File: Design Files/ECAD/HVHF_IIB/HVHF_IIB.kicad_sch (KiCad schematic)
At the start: 53 parts, among them J1 1984963, J2 1984963, J3 731375003, J4 CONSMA002-L, Q1 PNP, Q2 BFP196E6327HTSA1, T1 BFU590G, T10 BFQ252, T11 BFQ252, T12 BFQ252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

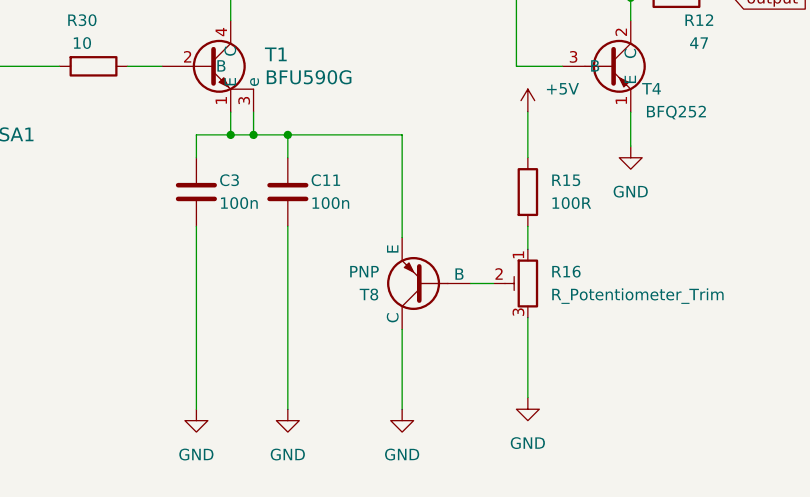
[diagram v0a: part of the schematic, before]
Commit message: adds footprints
3d models
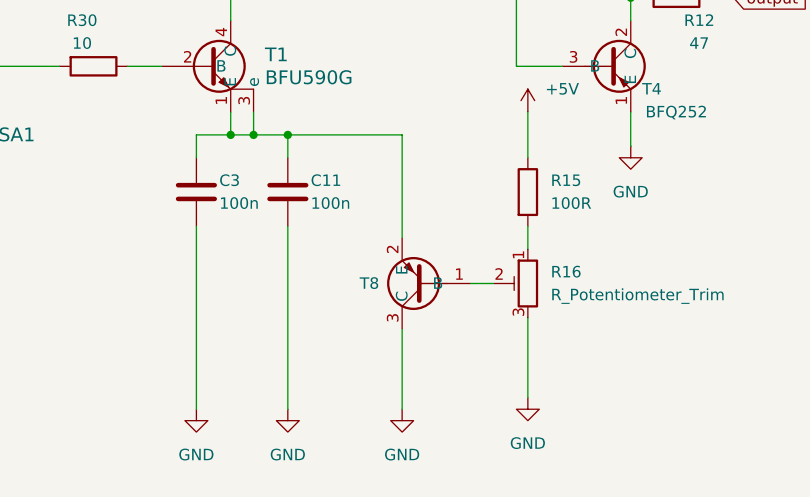
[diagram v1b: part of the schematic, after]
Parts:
- removed T8: PNP, symbol Simulation_SPICE:PNP
- added T8: ~, Package_TO_SOT_SMD:SOT-23, symbol New_Library:PMBT2907A
- R11: footprint Library:PWR163 DPAK -> Library:PWWR0016
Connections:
- net GND: now also T8.3 (C)
- net at R16.2: now also T8.1 (B)
- net at C11.1, C3.1, T1.1 (E)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: now also T8.2 (E)
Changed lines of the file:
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@@
       (effects (font (size 1.27 1.27)) (justify left))
     )
-    (property "Footprint" "Library:PWR163 DPAK" (at 104.902 91.44 90)
+    (property "Footprint" "Library:PWWR0016" (at 104.902 91.44 90)
       (effects (font (size 1.27 1.27)) hide)
     )
@@
     )
   )
+  (symbol (lib_id "New_Library:PMBT2907A") (at 139.7 172.72 180) (unit 1)
+    (in_bom yes) (on_board yes) (dnp no) (fields_autoplaced)
+    (property "Reference" "T8" (at 135.89 172.72 0)
+      (effects (font (size 1.27 1.27)) (justify left))
+    )
+    (property "Value" "~" (at 139.7 172.72 0)
+      (effects (font (size 1.27 1.27)))
+    )
+    (property "Footprint" "Package_TO_SOT_SMD:SOT-23" (at 139.7 172.72 0)
+      (effects (font (size 1.27 1.27)) hide)
+    )
+    (property "Datasheet" "" (at 139.7 172.72 0)
+      (effects (font (size 1.27 1.27)) hide)
+    )
+    (pin "1")
+    (pin "2")
+    (pin "3")
+    (instances
+      (project "HVHF_IIB"
+        (path "/a4785c7b-64d4-4462-915b-801e602c6997"
+          (reference "T8") (unit 1)
+        )
+      )
+    )
+  )
   (symbol (lib_id "Device:R") (at 142.24 114.3 270) (unit 1)
     (in_bom yes) (on_board yes) (dnp no) (fields_autoplaced)
@@
         )
       )
-    )
-  )
-  (symbol (lib_id "Simulation_SPICE:PNP") (at 140.97 172.72 180) (unit 1)
-    (in_bom yes) (on_board yes) (dnp no)
-    (property "Reference" "T8" (at 135.89 173.99 0)
-      (effects (font (size 1.27 1.27)) (justify left))
-    )
-    (property "Value" "PNP" (at 135.89 171.45 0)
-      (effects (font (size 1.27 1.27)) (justify left))
-    )
-    (property "Footprint" "" (at 105.41 172.72 0)
-      (effects (font (size 1.27 1.27)) hide)
-    )
-    (property "Datasheet" "~" (at 105.41 172.72 0)
-      (effects (font (size 1.27 1.27)) hide)
-    )
-    (property "Sim.Device" "PNP" (at 140.97 172.72 0)
-      (effects (font (size 1.27 1.27)) hide)
-    )
-    (property "Sim.Type" "GUMMELPOON" (at 140.97 172.72 0)
-      (effects (font (size 1.27 1.27)) hide)
-    )
-    (property "Sim.Pins" "1=C 2=B 3=E" (at 140.97 172.72 0)
-      (effects (font (size 1.27 1.27)) hide)
-    )
-    (pin "1")
-    (pin "2")
-    (pin "3")
-    (instances
-      (project "HVHF_IIB"
-        (path "/a4785c7b-64d4-4462-915b-801e602c6997"
-          (reference "T8") (unit 1)
-        )
-      )

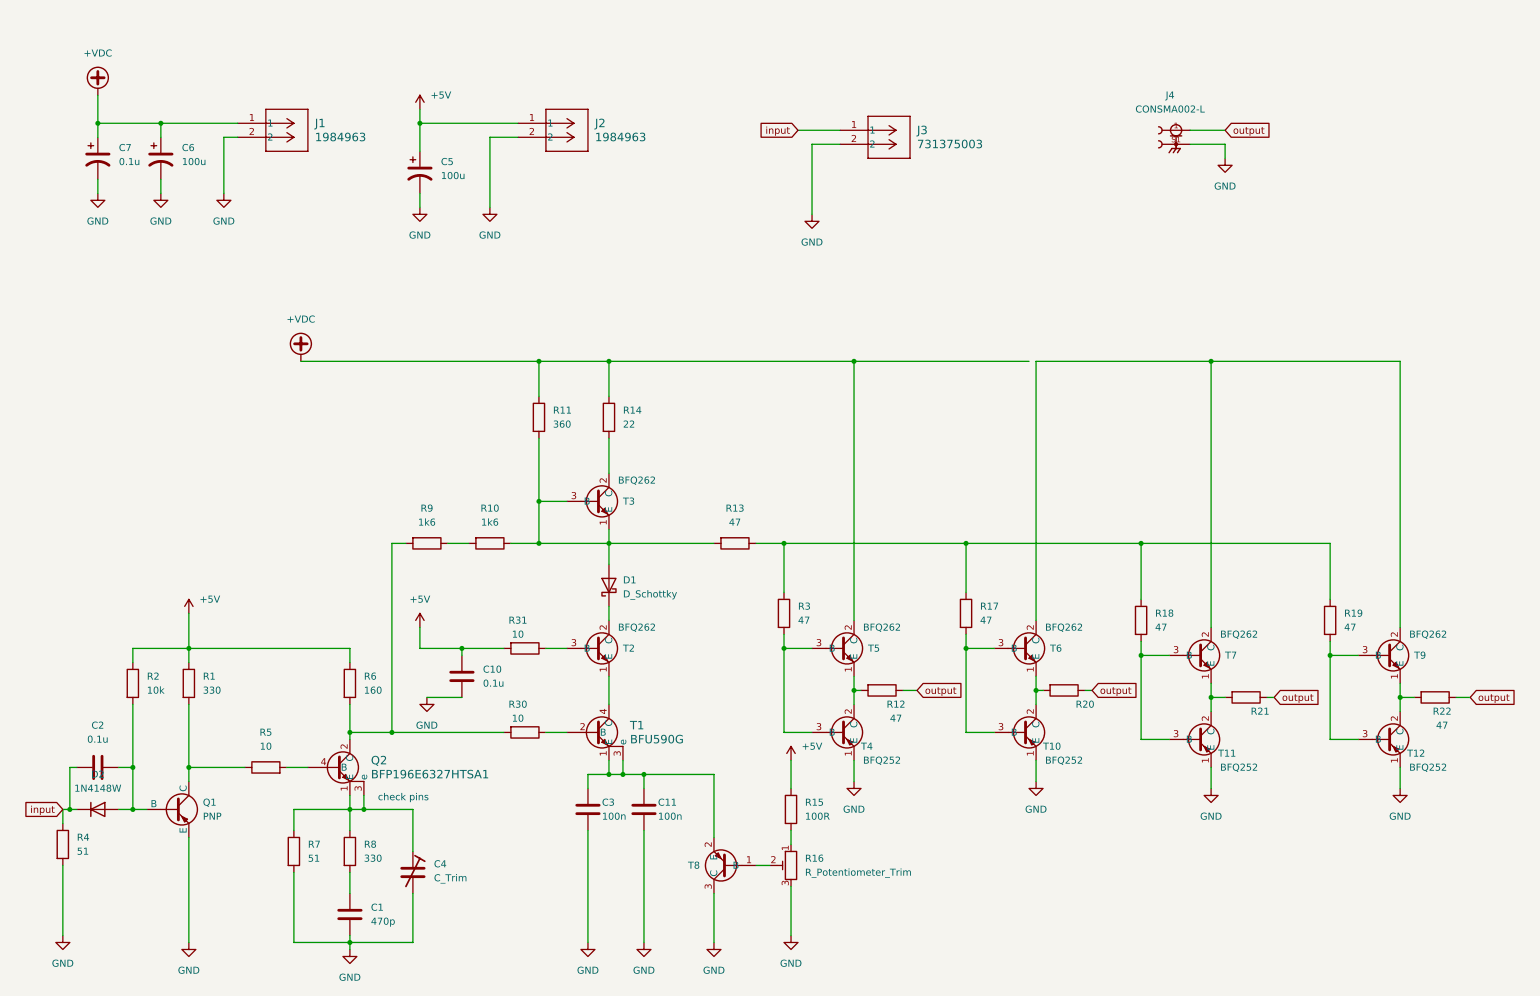
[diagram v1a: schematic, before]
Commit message: wrapped up schematic
placed and routed all components on schematic
adds all footprints
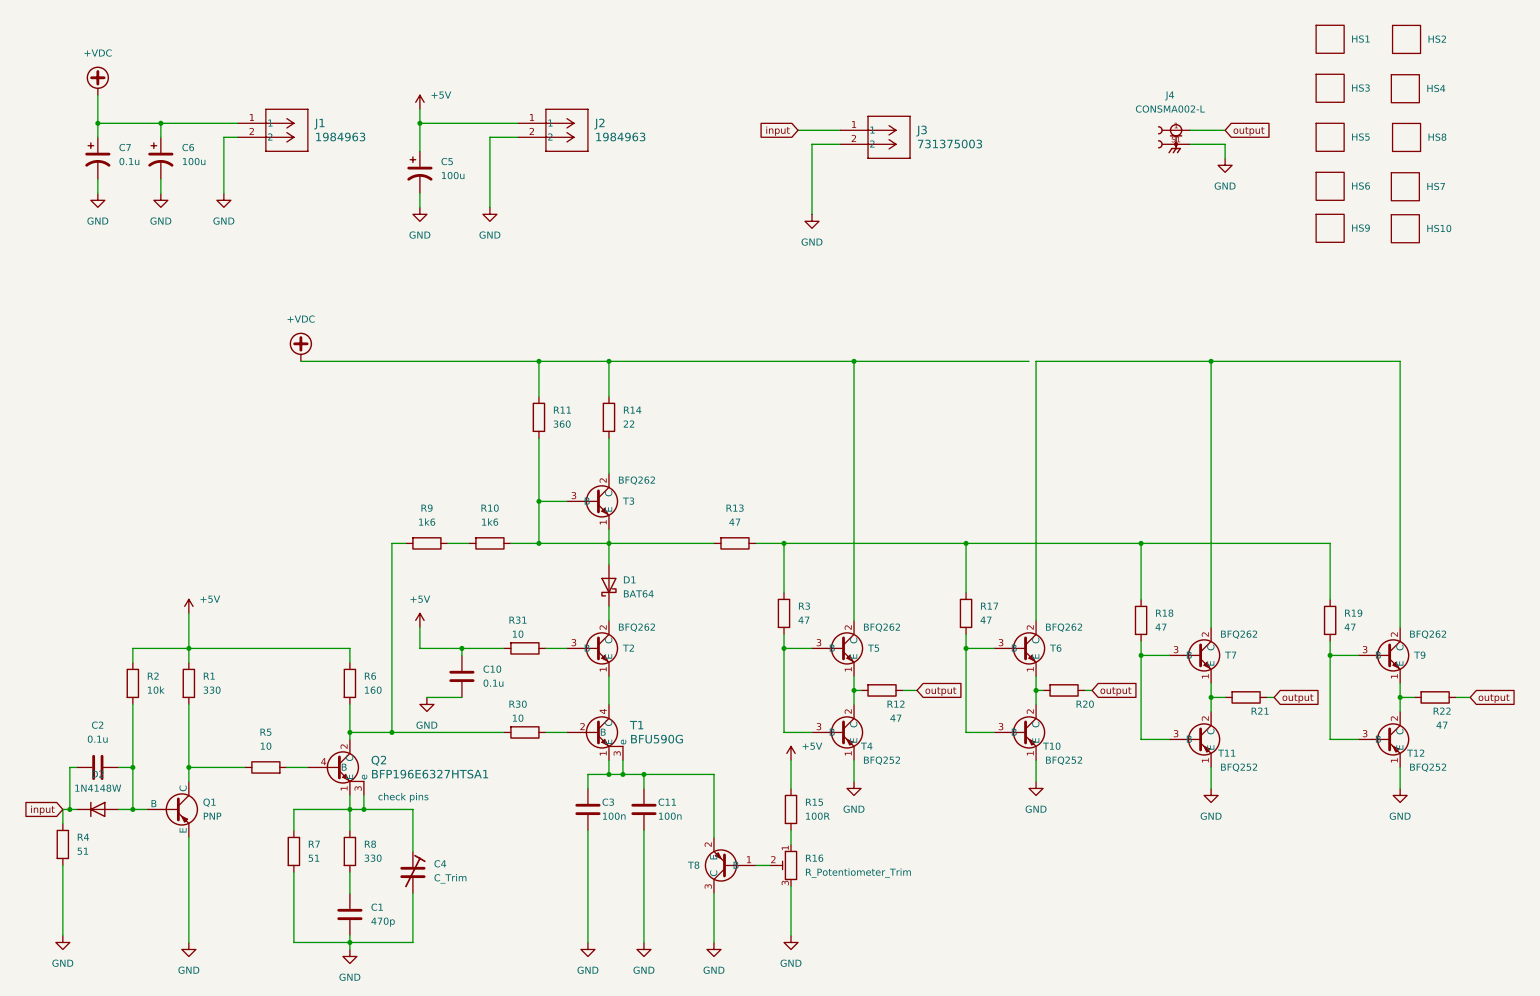
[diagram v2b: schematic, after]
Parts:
- added HS1, HS10, HS2, HS3, HS4, HS5, HS6, HS7, HS8, HS9: ~, Library:ATS_PCB1025, symbol New_Library:ATS-PCB1025
- C4: footprint (none) -> Library:PPZC80003
- C5, C7: footprint (none) -> Capacitor_SMD:C_1206_3216Metric_Pad1.33x1.80mm_HandSolder
- C6: footprint (none) -> Library:CAP_EEUED_125X25_PAN
- D1: value D_Schottky -> BAT64; footprint (none) -> Library:CR_BAS70-02V_INF-L

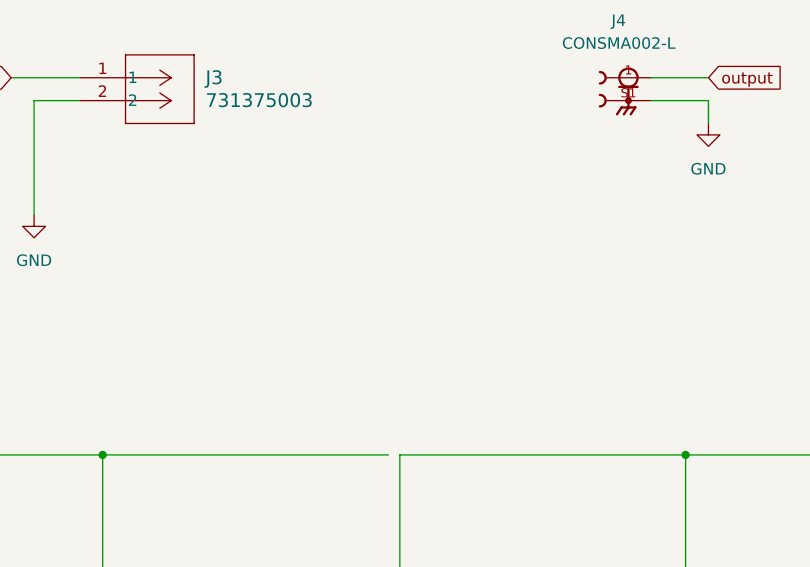
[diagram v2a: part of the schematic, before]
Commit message: PCB layout
adds bard logo
began pcb layout
adds 3D model heat sink
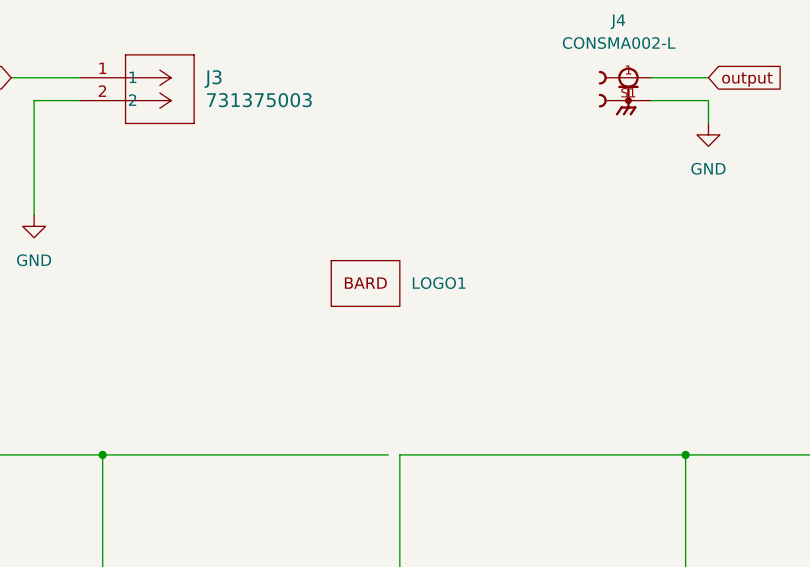
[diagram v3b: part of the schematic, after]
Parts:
- added LOGO1: ~, Library:Bard_Logo, symbol New_Library:BARD_LOGO
- T10, T11, T12, T2, T3, T4, T5, T6, T7, T9: footprint Package_TO_SOT_THT:TO-126-3_Horizontal_TabDown -> Library:TO126AV
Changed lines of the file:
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@@
       (effects (font (size 1.27 1.27)))
     )
-    (property "Footprint" "Package_TO_SOT_THT:TO-126-3_Horizontal_TabDown" (at 118.11 106.68 0)
+    (property "Footprint" "Library:TO126AV" (at 118.11 106.68 0)
       (effects (font (size 1.27 1.27)) hide)
     )
@@
       (effects (font (size 1.27 1.27)))
     )
-    (property "Footprint" "Package_TO_SOT_THT:TO-126-3_Horizontal_TabDown" (at 227.33 134.62 0)
+    (property "Footprint" "Library:TO126AV" (at 227.33 134.62 0)
       (effects (font (size 1.27 1.27)) hide)
     )
@@
       (effects (font (size 1.27 1.27)))
     )
-    (property "Footprint" "Package_TO_SOT_THT:TO-126-3_Horizontal_TabDown" (at 227.33 149.86 0)
+    (property "Footprint" "Library:TO126AV" (at 227.33 149.86 0)
       (effects (font (size 1.27 1.27)) hide)
     )
@@
       (effects (font (size 1.27 1.27)))
     )
-    (property "Footprint" "Package_TO_SOT_THT:TO-126-3_Horizontal_TabDown" (at 118.11 133.35 0)
+    (property "Footprint" "Library:TO126AV" (at 118.11 133.35 0)
       (effects (font (size 1.27 1.27)) hide)
     )
@@
       (effects (font (size 1.27 1.27)))
     )
-    (property "Footprint" "Package_TO_SOT_THT:TO-126-3_Horizontal_TabDown" (at 162.56 133.35 0)
+    (property "Footprint" "Library:TO126AV" (at 162.56 133.35 0)
       (effects (font (size 1.27 1.27)) hide)
     )
@@
       (effects (font (size 1.27 1.27)))
     )
-    (property "Footprint" "Package_TO_SOT_THT:TO-126-3_Horizontal_TabDown" (at 261.62 149.86 0)
+    (property "Footprint" "Library:TO126AV" (at 261.62 149.86 0)
       (effects (font (size 1.27 1.27)) hide)
     )
@@
     )
   )
+  (symbol (lib_id "New_Library:BARD_LOGO") (at 193.04 62.23 0) (unit 1)
+    (in_bom yes) (on_board yes) (dnp no) (fields_autoplaced)
+    (property "Reference" "LOGO1" (at 198.12 62.23 0)
+      (effects (font (size 1.27 1.27)) (justify left))
+    )
+    (property "Value" "~" (at 193.04 62.23 0)
+      (effects (font (size 1.27 1.27)))
+    )
+    (property "Footprint" "Library:Bard_Logo" (at 193.04 62.23 0)
+      (effects (font (size 1.27 1.27)) hide)
+    )
+    (property "Datasheet" "" (at 193.04 62.23 0)
+      (effects (font (size 1.27 1.27)) hide)
+    )
+    (instances
+      (project "HVHF_IIB"
+        (path "/a4785c7b-64d4-4462-915b-801e602c6997"
+          (reference "LOGO1") (unit 1)
+        )
+      )
+    )
+  )
   (symbol (lib_id "power:GND") (at 43.18 186.69 0) (unit 1)
     (in_bom yes) (on_board yes) (dnp no) (fields_autoplaced)
@@
       (effects (font (size 1.27 1.27)))
     )
-    (property "Footprint" "Package_TO_SOT_THT:TO-126-3_Horizontal_TabDown" (at 195.58 133.35 0)
+    (property "Footprint" "Library:TO126AV" (at 195.58 133.35 0)
       (effects (font (size 1.27 1.27)) hide)
     )
@@
       (effects (font (size 1.27 1.27)))
     )
-    (property "Footprint" "Package_TO_SOT_THT:TO-126-3_Horizontal_TabDown" (at 162.56 148.59 0)
+    (property "Footprint" "Library:TO126AV" (at 162.56 148.59 0)
       (effects (font (size 1.27 1.27)) hide)
     )
@@
       (effects (font (size 1.27 1.27)))
     )
-    (property "Footprint" "Package_TO_SOT_THT:TO-126-3_Horizontal_TabDown" (at 261.62 134.62 0)
+    (property "Footprint" "Library:TO126AV" (at 261.62 134.62 0)
       (effects (font (size 1.27 1.27)) hide)
     )
@@
       (effects (font (size 1.27 1.27)))
     )
-    (property "Footprint" "Package_TO_SOT_THT:TO-126-3_Horizontal_TabDown" (at 195.58 148.59 0)
-      (effects (font (size 1.27 1.27)) hide)
-    )
+    (property "Footprint" "Library:TO126AV" (at 195.58 148.59 0)
+      (effects (font (size 1.27 1.27)) hide)
+    )
